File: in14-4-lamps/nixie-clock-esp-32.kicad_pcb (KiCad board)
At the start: 2 copper layers, 100 x 50 mm, 65 parts, among them J1 Conn_01x02_Pin, J2 Conn_01x02_Pin, J3 Conn_01x06_Pin, Q1 MMBTA42, Q10 2N7002, Q2 MMBTA92, Q3 MMBTA42, Q4 MMBTA92, Q5 MMBTA42, Q6 MMBTA92, Q7 MMBTA42, Q8 MMBTA92, Q9 MMBTA42, U1 max688 boost regulator 5 to 1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, U2 AMS1117-3.3, U3 ESP32-WROOM-32D, U4 DS3231M, U5 74141

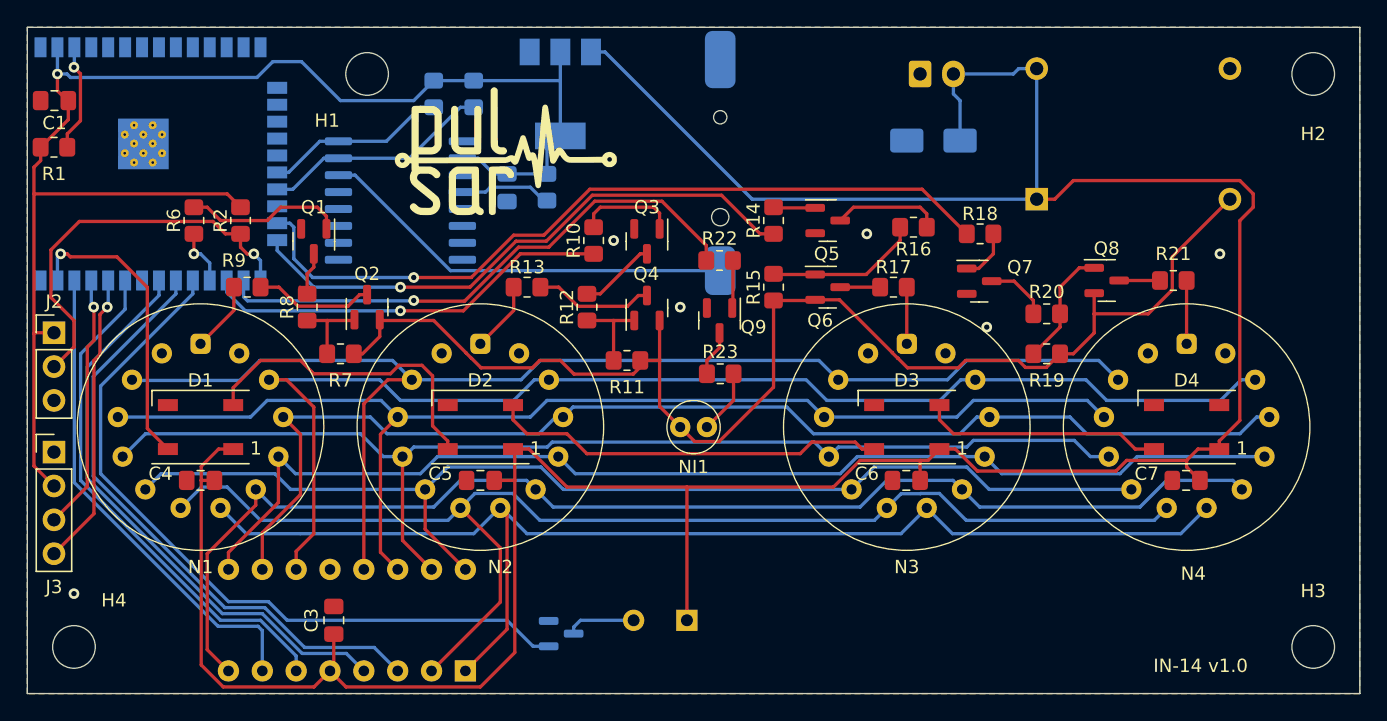
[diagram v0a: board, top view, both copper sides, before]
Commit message: add button and ws2812 connector
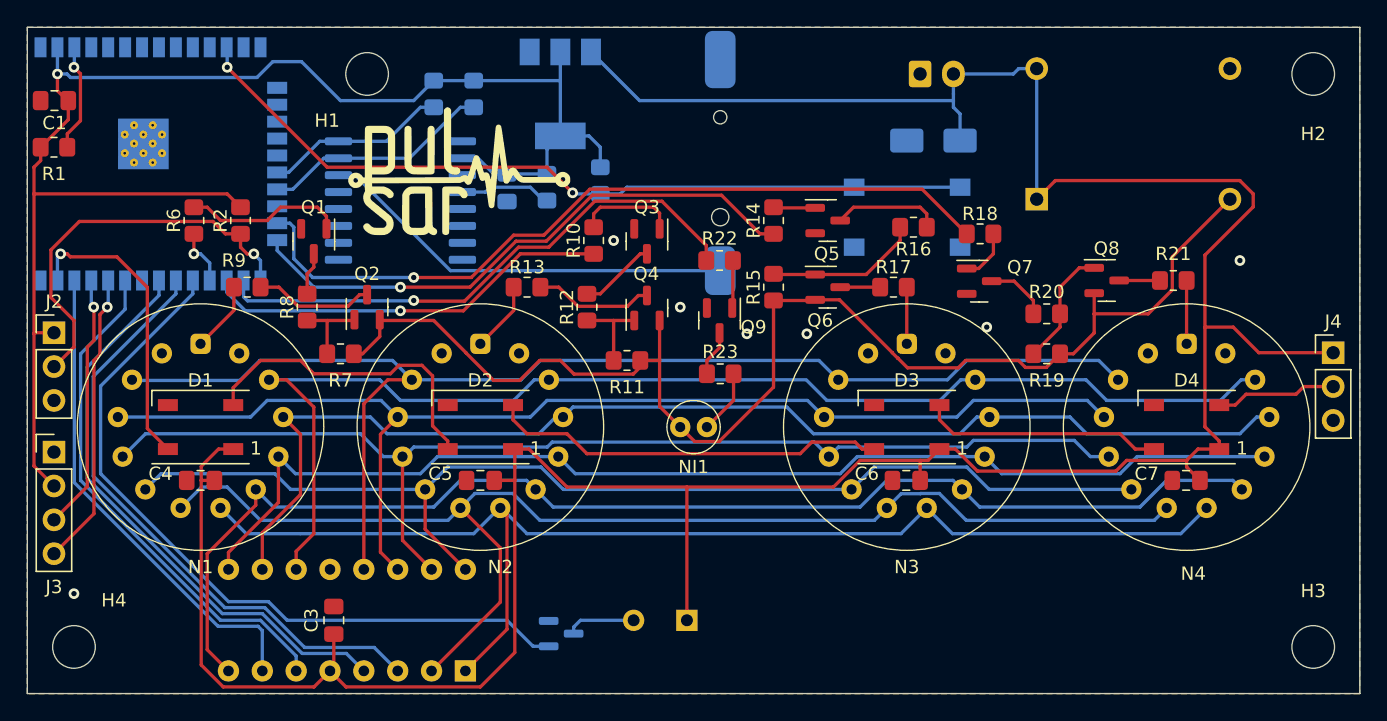
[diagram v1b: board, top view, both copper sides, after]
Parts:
- added J4: Conn_01x02_Pin, Connector_PinHeader_2.54mm:PinHeader_1x03_P2.54mm_Vertical, F.Cu at (148.0, 74.4)
- added R24: 10k, Resistor_SMD:R_0805_2012Metric_Pad1.20x1.40mm_HandSolder, B.Cu at (93.0, 61.5)
- added SW1: SW_Push, Button_Switch_SMD:SW_Push_1P1T_NO_6x6mm_H9.5mm, B.Cu at (116.0, 64.2)
- moved G*** 3.81 mm to (82.5, 61.0)
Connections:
- D4 pad 2: unconnected-(D4-DOUT-Pad2) -> Net-(D4-DOUT)
- U3 pad 12: unconnected-(U3-IO27-Pad12) -> /control/btn2
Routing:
- net /control/btn2: track 0.00 -> 60.7 mm, vias 0 -> 2
- net Net-(D4-DOUT): track 0.00 -> 9.13 mm
- net +3.3V: track 109.0 -> 113.9 mm
- net +5V: track 231.9 -> 234.0 mm
- net HV: track 98.1 -> 98.9 mm
- net GND: vias 6 -> 7
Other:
- board text added: "IP 192.168.4.1"
- board text added: "https://pulsarnixieclock.etsy.com"

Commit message: change in-14 footprint
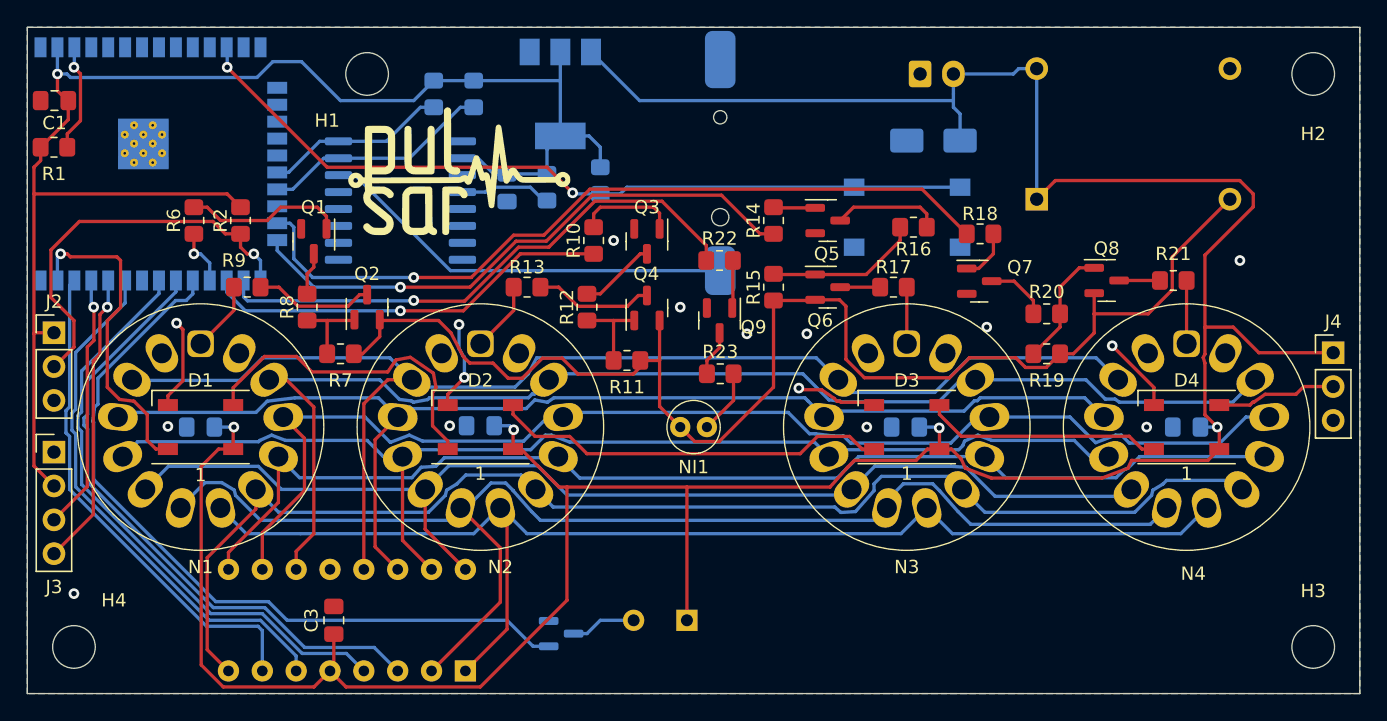
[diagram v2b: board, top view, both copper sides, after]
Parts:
- C4, C5, C6, C7: moved to B.Cu
- moved C5 4.10 mm to (84.0, 79.9)
- moved C6 4.00 mm to (115.9, 80.0)
- moved C7 4.00 mm to (137.0, 80.0)
- moved C4 4.00 mm to (63.0, 80.0)
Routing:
- net GND: track 0.00 -> 25.6 mm, vias 7 -> 16
- net +5V: track 234.0 -> 238.2 mm, vias 0 -> 4
- net HV: track 98.9 -> 102.4 mm
- net DIG5: track 95.0 -> 97.4 mm
- net DIG7: track 94.8 -> 96.8 mm
- net DIG9: track 90.9 -> 92.9 mm
- net DIG1: track 94.4 -> 96.4 mm
- net WS2812: track 22.4 -> 24.3 mm
- net /control/BUZZ: track 56.5 -> 57.9 mm
- net DIG3: track 87.2 -> 88.6 mm
- net DIG4: track 85.0 -> 86.3 mm
- net DEC0: track 46.1 -> 47.2 mm
- net DEC3: track 43.8 -> 44.9 mm
- net DIG2: track 89.6 -> 90.6 mm
- net DEC1: track 39.1 -> 40.2 mm
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
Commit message: add in-14 and in-16 6 lamp version
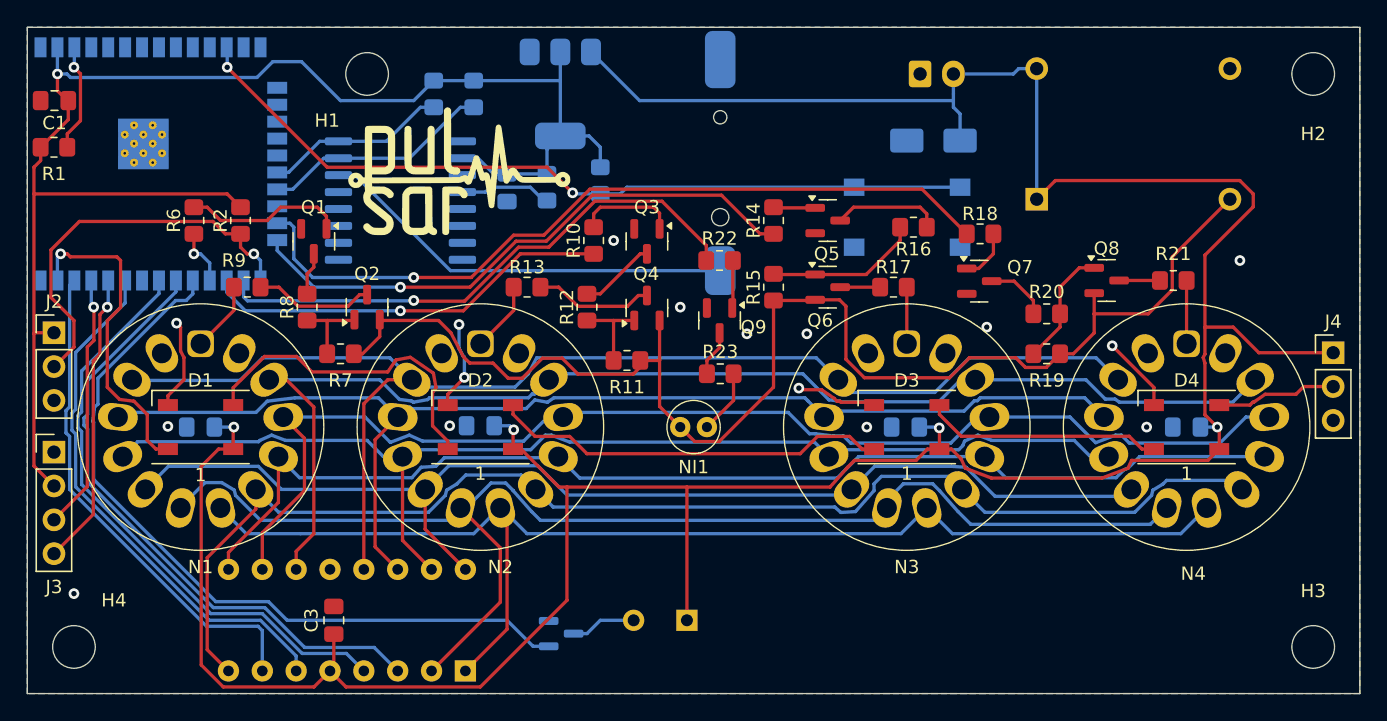
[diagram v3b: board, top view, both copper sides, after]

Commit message: fix i2c pins
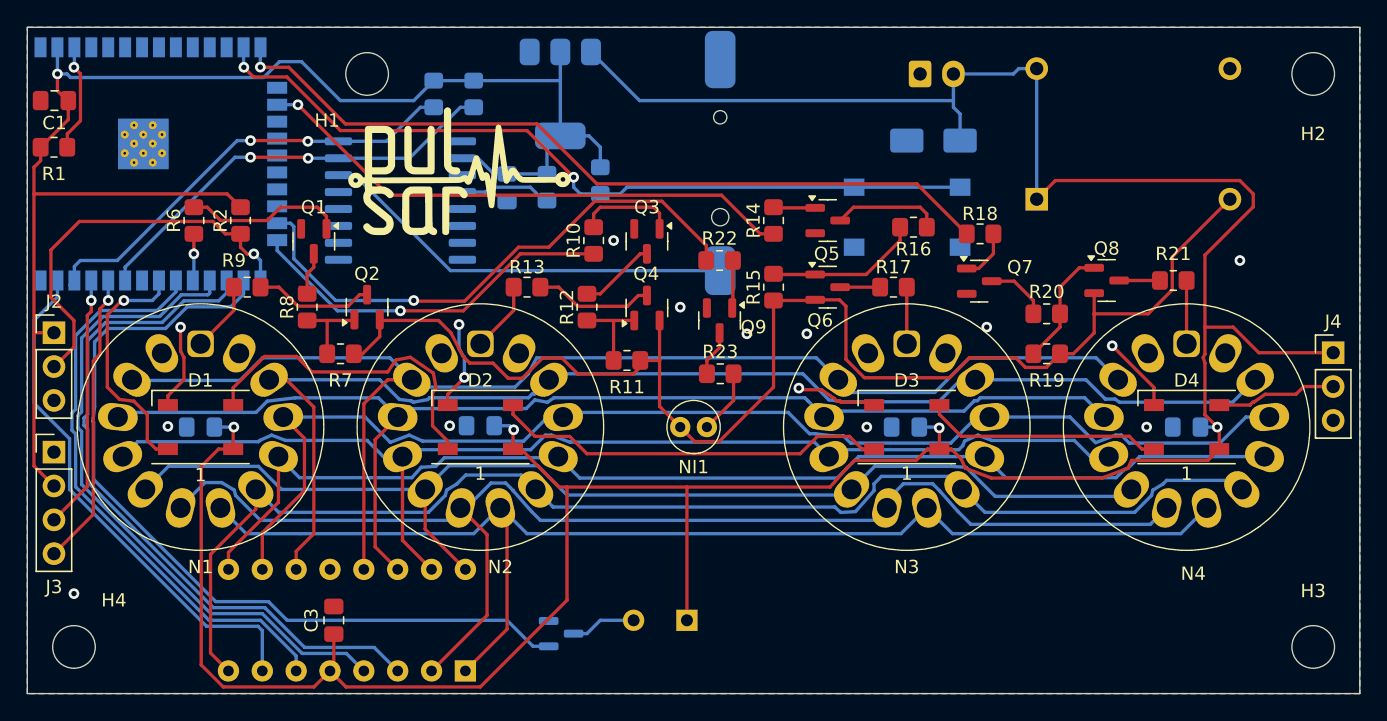
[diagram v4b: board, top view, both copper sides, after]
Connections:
- U3 pad 12: /control/btn2 -> unconnected-(U3-IO27-Pad12)
- U3 pad 13: unconnected-(U3-IO14-Pad13) -> /control/btn2
- U3 pad 14: unconnected-(U3-IO12-Pad14) -> A4
- U3 pad 16: unconnected-(U3-IO13-Pad16) -> A3
- U3 pad 20: /control/SCK -> unconnected-(U3-SCK/CLK-Pad20)
- U3 pad 21: /control/SDA -> unconnected-(U3-SDO/SD0-Pad21)
- U3 pad 23: A4 -> IN1
- U3 pad 24: A3 -> A2
- U3 pad 26: IN1 -> /control/BUZZ
- U3 pad 27: A2 -> DEC0
- U3 pad 28: A1 -> DEC3
- U3 pad 29: /control/BUZZ -> A1
- U3 pad 30: DEC0 -> DEC1
- U3 pad 31: DEC3 -> WS2812
- U3 pad 33: DEC1 -> /control/SDA
- U3 pad 36: DEC2 -> /control/SCK
- U3 pad 37: WS2812 -> DEC2
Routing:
- net /control/SCK: track 13.8 -> 33.5 mm, vias 0 -> 2
- net /control/SDA: track 17.3 -> 32.3 mm, vias 0 -> 2
- net WS2812: track 24.3 -> 18.5 mm
- net DEC0: track 47.2 -> 52.8 mm
- net /control/BUZZ: track 57.9 -> 63.4 mm
- net DEC3: track 44.9 -> 50.1 mm
- net DEC1: track 40.2 -> 44.3 mm
- net A2: track 30.8 -> 28.2 mm
- net A3: track 43.2 -> 41.3 mm
- net DEC2: track 37.9 -> 39.4 mm
- net DIG5: track 97.4 -> 96.5 mm
- net /control/btn2: track 60.7 -> 59.9 mm
- net A1: track 4.29 -> 3.53 mm
- net A4: track 59.0 -> 59.7 mm
